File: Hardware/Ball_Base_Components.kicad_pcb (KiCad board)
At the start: 2 copper layers, 42.5 x 100 mm, 61 parts, among them J1 Eurorack_10_pin_power, J2 SWD_Header, J3 USB_B_Micro, J4 X_Out, J5 Y_Out, J6 Z_Out, U1 STM32WB35, U2 MLPF-WB-01E3, U3 LD1117-3.3-4Tab, U4 TL072, U5 TL074, Y2 32MHz

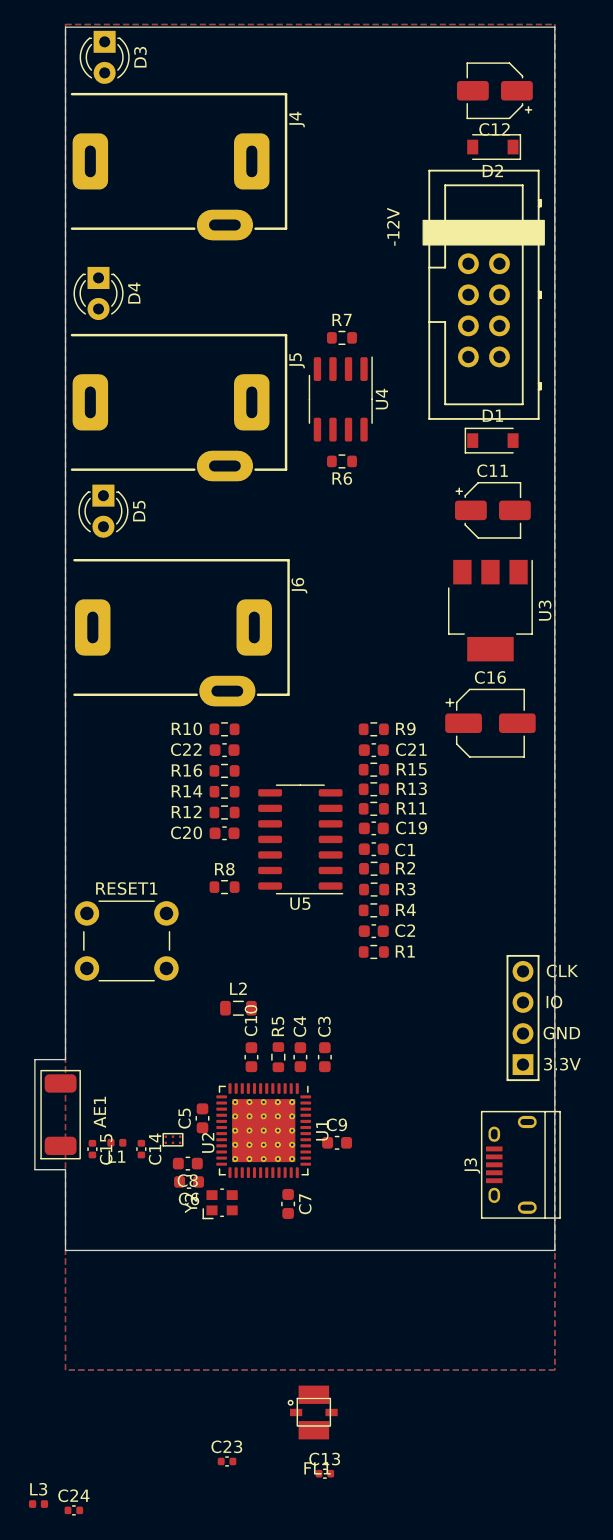
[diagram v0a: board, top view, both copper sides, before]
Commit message: First draft of Ball Base pcb completed
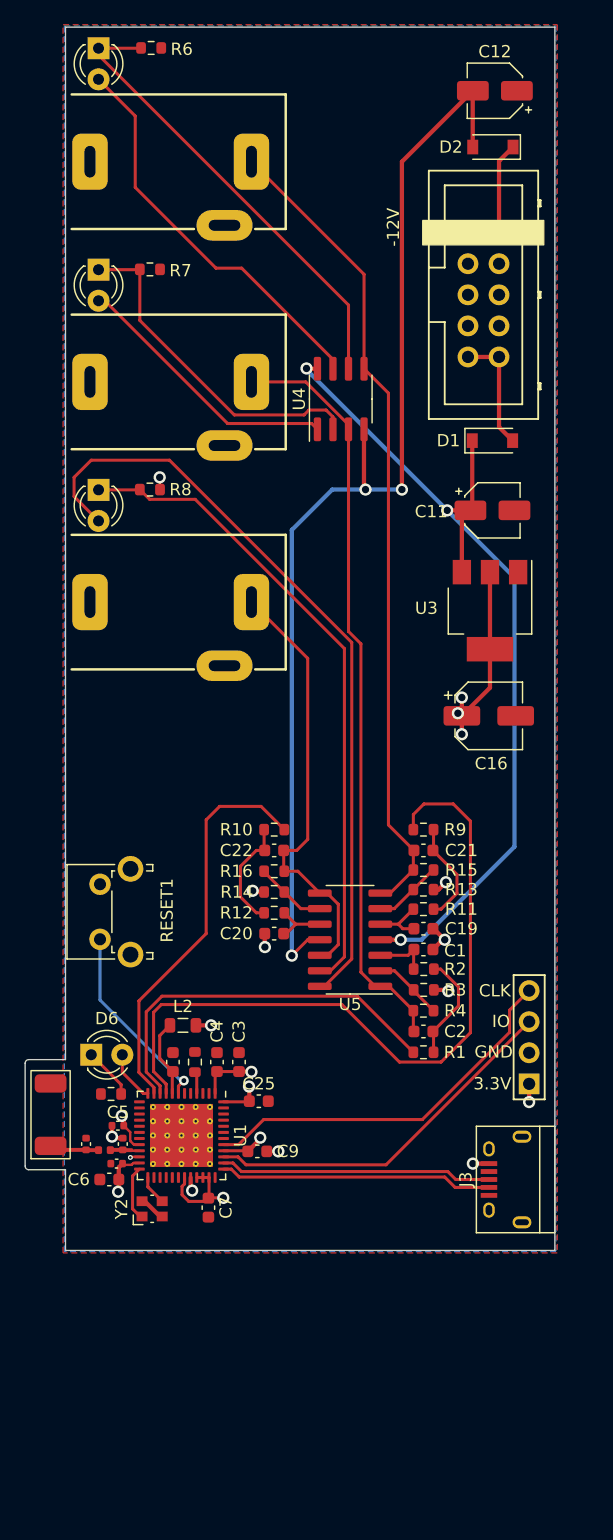
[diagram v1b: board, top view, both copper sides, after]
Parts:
- removed C13: 10nF, Capacitor_SMD:C_0402_1005Metric
- removed C23: DNF, Capacitor_SMD:C_0402_1005Metric
- removed C24: 1.2pF, Capacitor_SMD:C_0402_1005Metric
- removed FL1: Wurth_748351124, Custom_Footprints:Wurth_2.4GHz_Filter_2.5mm_2.0mm
- removed L3: 3.6nH, Inductor_SMD:L_0402_1005Metric
- removed U2: MLPF-WB-01E3, Custom_Footprints:MLPF-WB-01E3
- added C25: 100nF, Capacitor_SMD:C_0603_1608Metric, F.Cu at (141.4, 143.8)
- added D6: LED_BLUE, LED_THT:LED_D3.0mm_FlatTop, F.Cu at (127.7, 140.0)
- added R17: 1k, Resistor_SMD:R_0603_1608Metric, F.Cu at (129.3, 143.2)
- C14: value DNF -> 0.8pF
- C15: value 1.2pF -> 0.3pF
- C5, C8: footprint Capacitor_SMD:C_0603_1608Metric -> Capacitor_SMD:C_0402_1005Metric
- L1: value 3.6nH -> 2.7nH
- RESET1: footprint Custom_Footprints:SW_PUSH_6mm_aligned -> Button_Switch_THT:SW_Tactile_SPST_Angled_PTS645Vx58-2LFS
- moved R6 37.2 mm to (132.6, 57.7)
- moved R8 33.1 mm to (132.5, 93.8), turned to 180 degrees
- moved R7 16.7 mm to (132.5, 75.8), turned to 180 degrees
- moved R1 9.15 mm to (154.9, 139.8)
- moved R4 9.15 mm to (154.9, 136.4)
- moved C1 9.15 mm to (154.9, 131.4)
- moved C21 9.15 mm to (154.9, 123.3)
- moved C22 9.15 mm to (142.7, 123.3)
- moved R12 9.15 mm to (142.7, 128.4)
- moved R13 9.15 mm to (154.9, 126.5)
- moved R14 9.15 mm to (142.7, 126.7), turned to 0 degrees
- moved R15 9.15 mm to (154.9, 124.9)
- moved R16 9.15 mm to (142.7, 125.0)
- moved R2 9.15 mm to (154.9, 133.0)
- moved C19 9.15 mm to (154.9, 129.7)
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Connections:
- C14 pad 1: Net-(C14-Pad1) -> /RF_Output
- C2 pad 1: /X_Filtered -> /Y_Filtered
- C21 pad 1: /Y_Filtered -> /X_Filtered
- D3 pad 1: Net-(U5-Pad13) -> Net-(D3-Pad1)
- D3 pad 2: Net-(U5-Pad14) -> Net-(D3-Pad2)
- L1 pad 1: Net-(C14-Pad1) -> /RF_Output
- R1 pad 1: /X_PWM -> /Y_PWM
- R15 pad 2: /Y_Filtered -> /X_Filtered
- R4 pad 2: /X_Filtered -> /Y_Filtered
- R6 pad 2: Net-(D5-Pad1) -> Net-(D3-Pad1)
- R8 pad 2: Net-(U5-Pad13) -> Net-(D5-Pad1)
- R9 pad 1: /Y_PWM -> /X_PWM
- U1 pad 12: unconnected-(U1-Pad12) -> /LED_BLUE_OUT
- U4 pad 5: /Z_Filtered -> /X_Filtered
- U4 pad 6: Net-(D5-Pad1) -> Net-(D3-Pad1)
- U4 pad 7: Net-(D5-Pad2) -> Net-(D3-Pad2)
- U5 pad 1: /X_Filtered -> /Y_Filtered
- U5 pad 12: /X_Filtered -> /Z_Filtered
- U5 pad 13: Net-(U5-Pad13) -> Net-(D5-Pad1)
- U5 pad 14: Net-(U5-Pad14) -> Net-(D5-Pad2)
- U5 pad 7: /Y_Filtered -> /X_Filtered
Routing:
- net VEE: track 0.00 -> 92.6 mm, vias 0 -> 3
- net VCC: track 0.00 -> 74.2 mm, vias 0 -> 3
- net /X_Filtered: track 0.00 -> 66.9 mm
- net Net-(D5-Pad2): track 0.00 -> 63.3 mm
- net /Y_Filtered: track 0.00 -> 61.9 mm
- net /X_PWM: track 0.00 -> 60.3 mm
- net Net-(D5-Pad1): track 0.00 -> 53.2 mm
- net +3V3: track 0.00 -> 45.4 mm, vias 0 -> 11
- net Net-(D3-Pad1): track 0.00 -> 38.1 mm
- net /Z_Filtered: track 0.00 -> 36.1 mm
- net Net-(D3-Pad2): track 0.00 -> 32.8 mm
- net /Z_PWM: track 0.00 -> 32.8 mm
- net /Y_PWM: track 0.00 -> 31.4 mm
- net /SWCLK: track 0.00 -> 31.3 mm
- net /SWIO: track 0.00 -> 30.1 mm
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- added copper zone on In2.Cu, net +3V3
- added copper zone on In1.Cu, net GND
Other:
- board size 42.5 x 100 mm -> 43.3 x 100 mm
- copper layers 2 -> 4

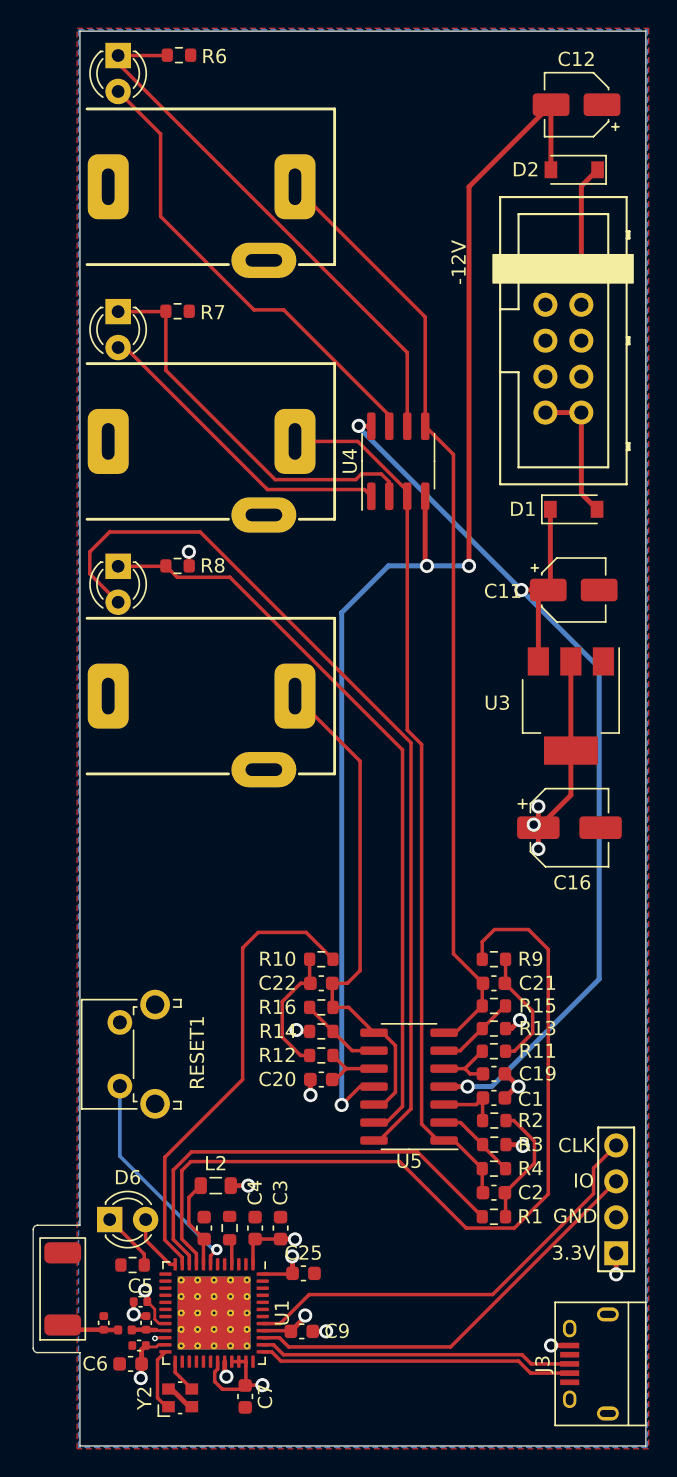
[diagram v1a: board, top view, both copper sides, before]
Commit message: Base PCB Updates and resize
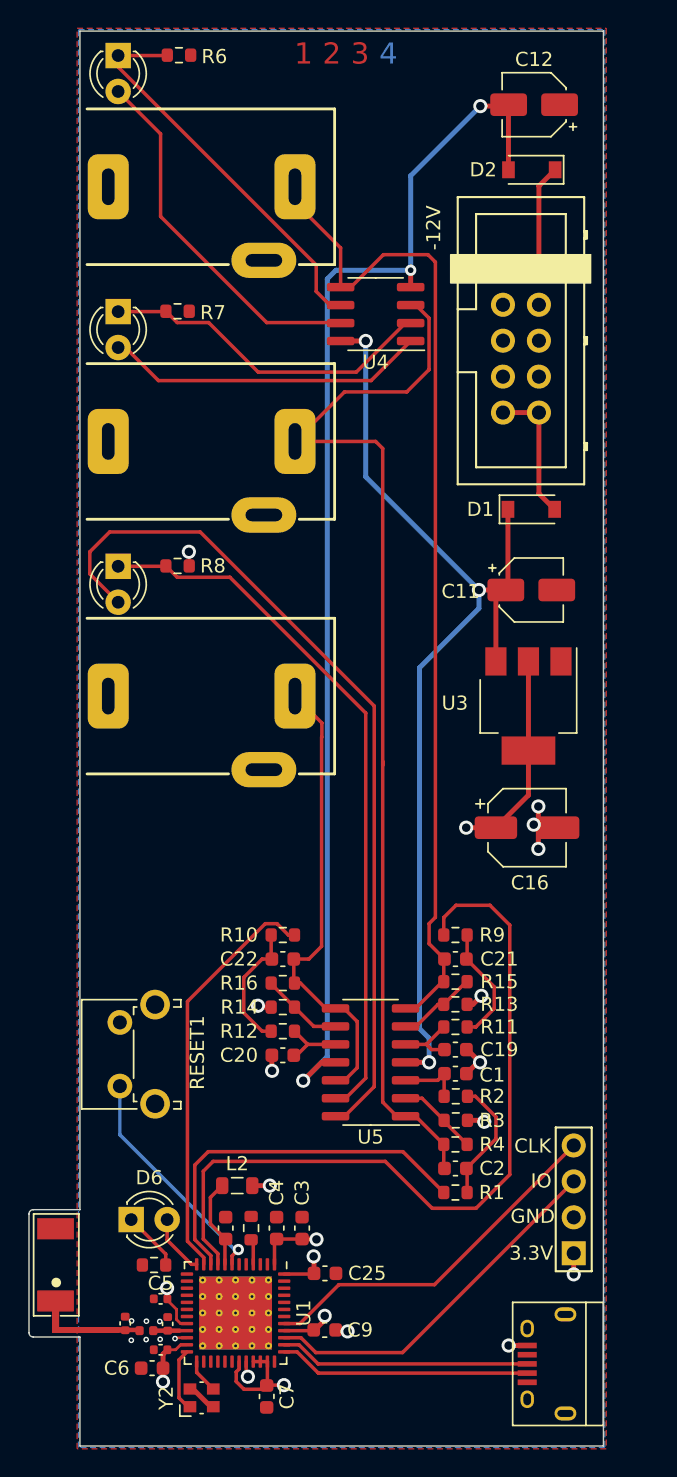
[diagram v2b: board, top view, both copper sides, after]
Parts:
- added FID1: Fiducial, Custom_Footprints:4_Layer_Markers, F.Cu at (144.4, 57.6)
- moved U4 10.5 mm to (146.5, 76.0), turned to 180 degrees
- moved AE1 4.06 mm to (128.4, 147.8)
- moved C1 3.22 mm to (152.1, 129.7)
- moved C2 3.22 mm to (152.1, 136.4)
- moved C21 3.22 mm to (152.1, 121.6)
- moved R1 3.22 mm to (152.1, 138.1)
- moved R13 3.22 mm to (152.1, 124.8)
- moved R15 3.22 mm to (152.1, 123.2)
- moved R4 3.22 mm to (152.1, 134.7)
- moved U5 3.22 mm to (146.1, 128.9)
- moved C19 3.22 mm to (152.1, 128.0)
- moved R11 3.22 mm to (152.1, 126.4)
- moved R9 3.22 mm to (152.1, 119.9)
- moved C20 3.22 mm to (139.9, 128.4)
- moved C22 3.22 mm to (139.9, 121.6)
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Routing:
- net /Y_Filtered: track 61.9 -> 77.1 mm
- net Net-(D3-Pad1): track 38.1 -> 28.1 mm
- net Net-(D3-Pad2): track 32.8 -> 25.9 mm
- net /SWCLK: track 31.3 -> 25.7 mm
- net VEE: track 92.6 -> 87.8 mm
- net /Y_PWM: track 31.4 -> 26.7 mm
- net /USB_DP: track 22.3 -> 17.7 mm
- net /USB_DM: track 22.3 -> 17.8 mm
- net /X_PWM: track 60.3 -> 55.8 mm
- net /X_Filtered: track 66.9 -> 71.3 mm
- net /SWIO: track 30.1 -> 25.9 mm
- net Net-(D4-Pad1): track 28.0 -> 23.9 mm
- net /Z_PWM: track 32.8 -> 29.2 mm
- net Net-(AE1-Pad1): track 4.06 -> 0.98 mm
- net Net-(D5-Pad2): track 63.3 -> 60.3 mm
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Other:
- board size 43.3 x 100 mm -> 40.6 x 100 mm

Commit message: Base - started panel PCB
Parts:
- added C13: 100nF, Capacitor_SMD:C_0603_1608Metric, F.Cu at (152.9, 125.8)
- added C17: 100nF, Capacitor_SMD:C_0603_1608Metric, F.Cu at (140.7, 124.1)
- added CONNECT1: SW_Push, Button_Switch_THT:SW_Tactile_SPST_Angled_PTS645Vx58-2LFS, F.Cu at (128.4, 131.1)
- added Ref**: Push_Button_Hole, Custom_Footprints:Small_Pushbutton_Hole_3.5mm, F.Cu at (110.0, 114.8)
- added Ref**: Oval_Mounting_Hole, Custom_Footprints:Oval_Mounting_Hole, F.Cu at (107.5, 165.0)
- added Ref**: LED_Hole_3mm, Custom_Footprints:LED_Hole_3mm, F.Cu at (110.0, 59.2)
- added Ref**: LED_Hole_3mm, Custom_Footprints:LED_Hole_3mm, F.Cu at (110.0, 95.3)
- added Ref**: LED_Hole_3mm, Custom_Footprints:LED_Hole_3mm, F.Cu at (110.0, 77.3)
- added Ref**: Push_Button_Hole, Custom_Footprints:Small_Pushbutton_Hole_3.5mm, F.Cu at (110.0, 128.8)
- added Ref**: Thonkikonn_6.1mm, Custom_Footprints:MountingHole_6.1mm, F.Cu at (110.0, 67.0)
- added Ref**: Oval_Mounting_Hole, Custom_Footprints:Oval_Mounting_Hole, F.Cu at (112.5, 42.5)
- added Ref**: Thonkikonn_6.1mm, Custom_Footprints:MountingHole_6.1mm, F.Cu at (110.0, 85.0)
- added Ref**: Thonkikonn_6.1mm, Custom_Footprints:MountingHole_6.1mm, F.Cu at (110.0, 103.0)
- added TP1: TestPoint, Custom_Footprints:1.3mm_Test_Point, F.Cu at (160.5, 124.6)
- added TP2: TestPoint, Custom_Footprints:1.3mm_Test_Point, F.Cu at (160.5, 117.2)
- added TP3: TestPoint, Custom_Footprints:1.3mm_Test_Point, F.Cu at (149.8, 94.0)
- added TP4: TestPoint, Custom_Footprints:1.3mm_Test_Point, F.Cu at (144.7, 94.0)
- moved R9 17.0 mm to (140.7, 132.5)
- moved C2 13.5 mm to (140.7, 129.2), turned to 180 degrees
- moved R1 13.5 mm to (140.7, 130.9)
- moved RESET1 13.5 mm to (128.4, 117.1)
- moved R10 7.65 mm to (140.7, 127.5), turned to 0 degrees
- moved R16 6.05 mm to (140.8, 117.3)
- moved R12 6.03 mm to (140.7, 120.7)
- moved R14 6.03 mm to (140.7, 119.0)
- moved C20 6.03 mm to (140.7, 122.4)
- moved D2 5.72 mm to (159.7, 60.5), turned to 90 degrees
- moved C11 5.33 mm to (155.2, 90.7), turned to 90 degrees
- moved C21 4.40 mm to (152.9, 117.3)
- moved R15 4.31 mm to (152.9, 119.0)
- moved C22 4.28 mm to (140.7, 125.8)
- moved R13 4.21 mm to (152.9, 120.7)
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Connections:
- U1 pad 13: unconnected-(U1-Pad13) -> /CONNECT
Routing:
- net /X_PWM: track 55.8 -> 13.8 mm
- net Net-(C21-Pad2): track 8.49 -> 40.2 mm
- net Net-(C2-Pad2): track 8.85 -> 24.8 mm
- net /CONNECT: track 0.00 -> 14.7 mm
- net /RESET: track 16.4 -> 29.8 mm
- net /Y_PWM: track 26.7 -> 15.8 mm
- net /Z_PWM: track 29.2 -> 18.8 mm
- net VEE: track 87.8 -> 82.1 mm
- net /X_Filtered: track 71.3 -> 66.1 mm
- net +3V3: track 43.9 -> 39.8 mm
- net VCC: track 72.8 -> 69.0 mm
- net Net-(D5-Pad1): track 50.3 -> 46.8 mm
- net Net-(D5-Pad2): track 60.3 -> 57.3 mm
- net +12V: track 9.84 -> 11.6 mm
- net GND: track 17.9 -> 16.2 mm, vias 19 -> 25
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- added copper zone on F.Cu, net +3V3
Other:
- board size 40.6 x 100 mm -> 62.6 x 128.5 mm
- board text added: "+12V"
- board text added: "-12V"
- board text added: "3.3V"
- board text added: "Antenna"
- board text added: "Connect"
- board text added: "GND"
- board text added: "LED X"
- board text added: "LED Y"
- board text added: "LED Z"
- board text added: "Reset"
- board text added: "X Out"
- board text added: "Y Out"
- board text added: "Z Out"

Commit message: Minor PCB Updates
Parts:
- moved TP2 0.30 mm to (160.5, 117.5)
- moved U5 0.15 mm to (146.8, 125.0)
- moved R16 0.11 mm to (140.7, 117.3)
- moved R4 0.10 mm to (152.9, 132.6)
- moved R9 0.10 mm to (140.7, 132.6)
- moved U4 0.10 mm to (146.8, 76.0)
- moved R2 0.09 mm to (152.9, 129.2)
- moved C1 0.07 mm to (152.9, 127.5)
- moved C21 0.07 mm to (152.9, 117.3)
- moved R11 0.07 mm to (152.9, 122.4)
- moved R13 0.07 mm to (152.9, 120.7)
- moved R15 0.07 mm to (152.9, 119.0)
- moved C19 0.07 mm to (152.9, 124.1)
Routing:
- net /Z_Filtered: track 34.2 -> 36.3 mm
- net VEE: track 82.1 -> 81.1 mm
- net Net-(C19-Pad2): track 4.52 -> 5.02 mm

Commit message: More PCB Clean up
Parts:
- removed the Ref** at (110.0, 114.8)
- removed the Ref** at (107.5, 165.0)
- removed the Ref** at (110.0, 59.2)
- removed the Ref** at (110.0, 95.3)
- removed the Ref** at (110.0, 77.3)
- removed the Ref** at (110.0, 128.8)
- removed the Ref** at (110.0, 67.0)
- removed the Ref** at (112.5, 42.5)
- removed the Ref** at (110.0, 85.0)
- removed the Ref** at (110.0, 103.0)
- added Ref**: Thonkikonn_6.1mm, Custom_Footprints:MountingHole_6.1mm, F.Cu at (80.3, 85.0)
- added Ref**: LED_Hole_3mm, Custom_Footprints:LED_Hole_3mm, F.Cu at (80.3, 77.3)
- added Ref**: Oval_Mounting_Hole, Custom_Footprints:Oval_Mounting_Hole, F.Cu at (77.8, 165.0)
- added Ref**: LED_Hole_3mm, Custom_Footprints:LED_Hole_3mm, F.Cu at (80.3, 95.3)
- added Ref**: Thonkikonn_6.1mm, Custom_Footprints:MountingHole_6.1mm, F.Cu at (80.3, 103.0)
- added Ref**: LED_Hole_3mm, Custom_Footprints:LED_Hole_3mm, F.Cu at (80.3, 59.2)
- added Ref**: Push_Button_Hole, Custom_Footprints:Small_Pushbutton_Hole_3.5mm, F.Cu at (80.3, 128.8)
- added Ref**: Push_Button_Hole, Custom_Footprints:Small_Pushbutton_Hole_3.5mm, F.Cu at (80.3, 114.8)
- added Ref**: Oval_Mounting_Hole, Custom_Footprints:Oval_Mounting_Hole, F.Cu at (82.8, 42.5)
- added Ref**: Thonkikonn_6.1mm, Custom_Footprints:MountingHole_6.1mm, F.Cu at (80.3, 67.0)
- FID1: value Fiducial -> 4 Layer Marker
- moved R14 61.8 mm to (152.6, 116.1)
- moved R15 51.1 mm to (140.4, 126.3)
- moved U4 41.0 mm to (146.5, 117.0), turned to 0 degrees
- moved R16 22.1 mm to (140.4, 114.4), turned to 0 degrees
- moved C21 6.31 mm to (140.4, 119.5), turned to 0 degrees
- moved R10 6.31 mm to (140.4, 121.2)
- moved C15 3.91 mm to (140.4, 128.0)
- moved U3 3.51 mm to (146.5, 128.5)
- moved C16 2.22 mm to (152.6, 128.0)
- moved R11 2.22 mm to (140.4, 122.9)
- moved C22 2.22 mm to (140.4, 124.6)
- moved C18 1.24 mm to (152.6, 126.3)
- moved R12 1.24 mm to (140.4, 116.1)
- moved R13 1.24 mm to (140.4, 117.8)
- moved TP4 0.70 mm to (144.0, 94.0)
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- renumbered C3 to C1, C11 to C10, C12 to C11, C14 to C12, C15 to C13, C16 to C14, C17 to C15, C13 to C16, C2 to C17, C1 to C18, C21 to C19, C4 to C2, C19 to C20, C22 to C21, C20 to C22, C5 to C3, C7 to C4, C25 to C5, C9 to C6, C10 to C7, C6 to C8, C8 to C9, D6 to D3, D3 to D4, D4 to D5, D5 to D6, R5 to R1, R12 to R11, R16 to R12, R14 to R13, R6 to R14, R7 to R15, R8 to R16, R1 to R2, R2 to R3, R3 to R5, R9 to R6, R11 to R7, R15 to R8, R13 to R9, U3 to U2, U5 to U3, Y2 to Y1
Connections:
- D5 pad 1: Net-(D4-Pad1) (its old number) -> Net-(D5-Pad1)
- D5 pad 2: Net-(D4-Pad2) (its old number) -> Net-(D5-Pad2)
- D6 pad 1: Net-(D5-Pad1) -> Net-(D6-Pad1)
- D6 pad 2: Net-(D5-Pad2) -> Net-(D6-Pad2)
- R15 pad 2: Net-(D4-Pad1) (its old number) -> Net-(D5-Pad1)
- R16 pad 2: Net-(D5-Pad1) -> Net-(D6-Pad1)
- U3 pad 12: /Z_Filtered -> /Y_Filtered
- U4 pad 1: Net-(D4-Pad2) (its old number) -> Net-(D6-Pad2)
- U4 pad 2: Net-(D4-Pad1) (its old number) -> Net-(D6-Pad1)
- U4 pad 3: /Y_Filtered -> /Z_Filtered
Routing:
- net Net-(D4-Pad1): track 28.2 -> 72.8 mm
- net Net-(D6-Pad1): track 0.00 -> 41.0 mm
- net Net-(D4-Pad2): track 26.3 -> 66.1 mm
- net Net-(D6-Pad2): track 0.00 -> 32.3 mm
- net Net-(D4-Pad1) (its old number): track 23.7 -> 0.00 mm
- net Net-(D4-Pad2) (its old number): track 22.8 -> 0.00 mm
- net Net-(D5-Pad1): track 46.8 -> 66.2 mm, vias 0 -> 2
- net VCC: track 69.0 -> 55.9 mm
- net /Y_Filtered: track 78.0 -> 66.1 mm
- net Net-(D5-Pad2): track 57.3 -> 68.6 mm
- net /Z_PWM: track 18.8 -> 24.9 mm
- net Net-(C21-Pad2): track 9.16 -> 4.19 mm
- net VEE: track 81.1 -> 85.8 mm
- net Net-(R12-Pad1): track 7.46 -> 12.0 mm
- net Net-(C19-Pad2): track 40.1 -> 36.1 mm
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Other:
- board size 62.6 x 128.5 mm -> 92.3 x 128.5 mm
- board text added: "Ball Base v1.0 Mountjoy Modular 2022"
- board text added: "CONNECT"
- board text added: "RESET"
- board text removed: "Antenna"
- board text removed: "Connect"

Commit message: PCB Updates
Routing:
- net GND: track 15.5 -> 20.6 mm, vias 19 -> 80
- net /Y_Filtered: track 66.1 -> 65.4 mm
- net +3V3: vias 9 -> 15
- added copper zone on B.Cu, net +3V3
- added copper zone on In1.Cu, net +3V3
